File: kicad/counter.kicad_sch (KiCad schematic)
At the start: 2 parts, among them U2 SN74HCS72QDRQ1, U3 74AHC1G00

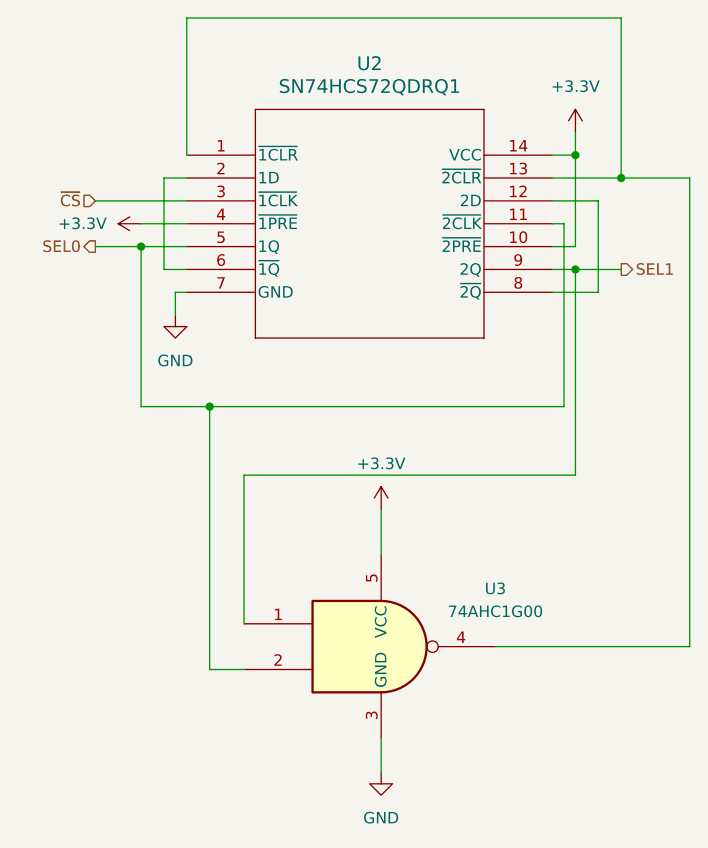
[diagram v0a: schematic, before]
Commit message: finish schematic for amp, and start routing (schematic isn't actually fully connected yet tho...)
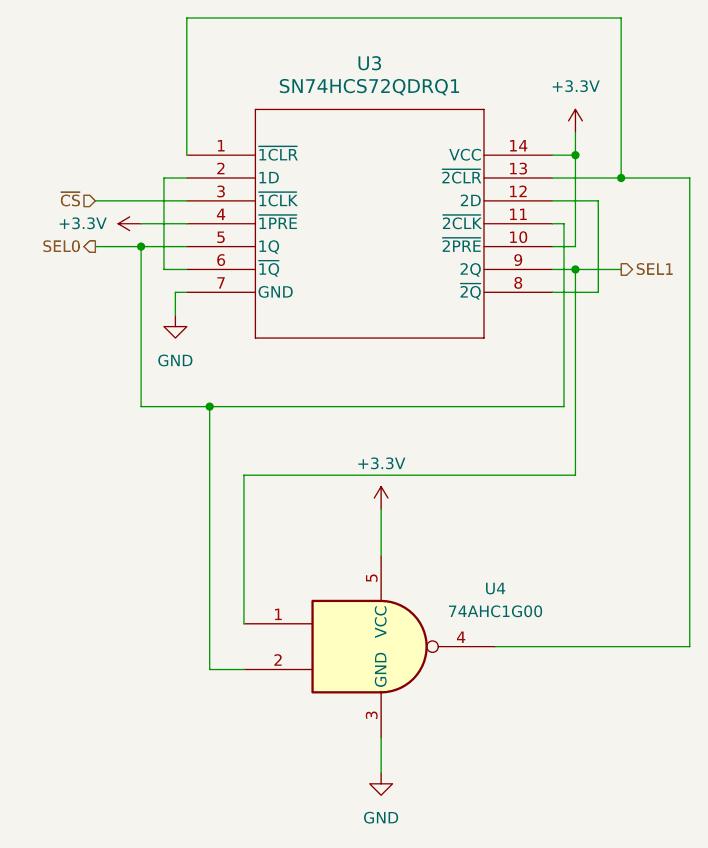
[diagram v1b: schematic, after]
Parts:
- U3: renamed from U2; footprint SOIC_QDRQ1_TEX -> strain-gauge:SOIC_QDRQ1_TEX
- U4: renamed from U3; footprint (none) -> Package_TO_SOT_SMD:SOT-353_SC-70-5
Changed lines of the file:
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@@
 		(dnp no)
 		(fields_autoplaced yes)
-		(property "Reference" "U3"
+		(property "Reference" "U4"
 			(at 139.7 145.9798 0)
 			(effects
@@
 			)
 		)
-		(property "Footprint" ""
+		(property "Footprint" "Package_TO_SOT_SMD:SOT-353_SC-70-5"
 			(at 127 152.4 0)
 			(effects
@@
 			(project "strain-gauge"
 				(path "/cbc99ef0-5fa7-4678-bd4c-c2c08fe588b6/b13d2ad6-b452-4e9e-8747-b60d4710f9cf"
-					(reference "U3")
+					(reference "U4")
 					(unit 1)
 				)
@@
 		(dnp no)
 		(fields_autoplaced yes)
-		(property "Reference" "#PWR07"
+		(property "Reference" "#PWR013"
 			(at 148.59 99.06 0)
 			(effects
@@
 			(project ""
 				(path "/cbc99ef0-5fa7-4678-bd4c-c2c08fe588b6/b13d2ad6-b452-4e9e-8747-b60d4710f9cf"
-					(reference "#PWR07")
+					(reference "#PWR013")
 					(unit 1)
 				)
@@
 		(dnp no)
 		(fields_autoplaced yes)
-		(property "Reference" "#PWR08"
+		(property "Reference" "#PWR09"
 			(at 104.14 105.41 0)
 			(effects
@@
 			(project ""
 				(path "/cbc99ef0-5fa7-4678-bd4c-c2c08fe588b6/b13d2ad6-b452-4e9e-8747-b60d4710f9cf"
-					(reference "#PWR08")
+					(reference "#PWR09")
 					(unit 1)
 				)
@@
 		(dnp no)
 		(fields_autoplaced yes)
-		(property "Reference" "#PWR09"
+		(property "Reference" "#PWR011"
 			(at 127 140.97 0)
 			(effects
@@
 			(project ""
 				(path "/cbc99ef0-5fa7-4678-bd4c-c2c08fe588b6/b13d2ad6-b452-4e9e-8747-b60d4710f9cf"
-					(reference "#PWR09")
+					(reference "#PWR011")
 					(unit 1)
 				)
@@
 		(dnp no)
 		(fields_autoplaced yes)
-		(property "Reference" "#PWR05"
+		(property "Reference" "#PWR010"
 			(at 104.14 121.92 0)
 			(effects
@@
 			(project ""
 				(path "/cbc99ef0-5fa7-4678-bd4c-c2c08fe588b6/b13d2ad6-b452-4e9e-8747-b60d4710f9cf"
-					(reference "#PWR05")
+					(reference "#PWR010")
 					(unit 1)
 				)
@@
 		(dnp no)
 		(fields_autoplaced yes)
-		(property "Reference" "U2"
+		(property "Reference" "U3"
 			(at 125.73 87.63 0)
 			(effects
@@
 			)
 		)
-		(property "Footprint" "SOIC_QDRQ1_TEX"
+		(property "Footprint" "strain-gauge:SOIC_QDRQ1_TEX"
 			(at 105.41 97.79 0)
 			(effects
@@
 			(project "strain-gauge"
 				(path "/cbc99ef0-5fa7-4678-bd4c-c2c08fe588b6/b13d2ad6-b452-4e9e-8747-b60d4710f9cf"
-					(reference "U2")
+					(reference "U3")
 					(unit 1)
 				)
@@
 		(dnp no)
 		(fields_autoplaced yes)
-		(property "Reference" "#PWR010"
+		(property "Reference" "#PWR012"
 			(at 127 172.72 0)
 			(effects
@@
 			(project ""
 				(path "/cbc99ef0-5fa7-4678-bd4c-c2c08fe588b6/b13d2ad6-b452-4e9e-8747-b60d4710f9cf"
-					(reference "#PWR010")
-					(unit 1)
-				)
+					(reference "#PWR012")
+					(unit 1)
+				)
